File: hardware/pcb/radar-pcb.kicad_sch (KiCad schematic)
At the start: 36 parts, among them J1 DC 5,5x2,5 mm (+ w srodku), J2 DevKit J1, J3 DevKit J3, J4 HC-SR04 (kabel): VCC TRIG ECH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, J5 Serwo SG90 (kabel): GND +5V S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, J6 MAX7219 Elegoo: VCC GND DIN C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, J7 OLED SH1106: VCC GND SCK SDA, J8 Buzzer: + -, J9 Przycisk zewnetrzny, Q1 AO3401A (P-MOSFET), Q2 MMBT3904, SW1 Przycisk ON/standby, U1 SN74AHCT125N

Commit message: PCB: routed two-layer board, DRC clean, one-command rebuild
66 x 128 mm board generated from the schematic netlist with planned
placement for all 36 parts, routed with Freerouting, GND pours on both
layers. DRC with schematic parity: 0 errors, 0 unconnected, 0 parity
issues (silkscreen warnings only). build_all.sh regenerates everything.

Co-Authored-By: Claude Opus 5.5 <noreply@anthropic.com>
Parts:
- TP1, TP2, TP3, TP4, TP5: now left out of the parts list

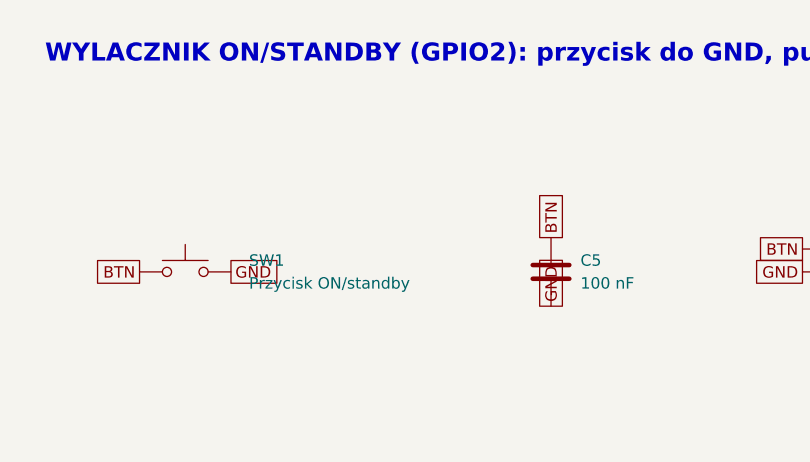
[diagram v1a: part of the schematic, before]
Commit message: PCB: silkscreen pin labels, side-actuated button, verification dimensions
Every connector is labelled with module and pin names, the DevKit sockets
with all 32 pin names on the back, parts with reference and value plus
polarity marks. ON/STANDBY uses a right-angle PTS645 switch at the left
edge. Dimensions W1-W12 to verify are drawn on Dwgs.User/Cmts.User for
the 1:1 verification PDF. DRC: 0 errors, schematic parity clean.

Co-Authored-By: Claude Opus 5.5 <noreply@anthropic.com>
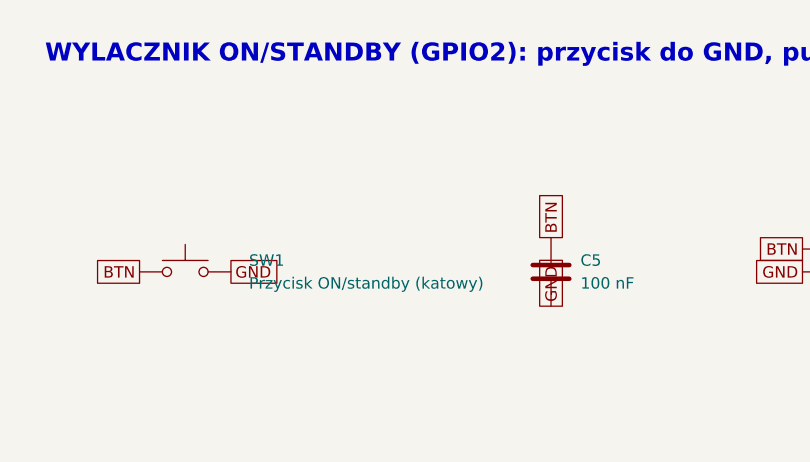
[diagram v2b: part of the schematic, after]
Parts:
- SW1: value Przycisk ON/standby -> Przycisk ON/standby (katowy); footprint Button_Switch_THT:SW_PUSH_6mm -> Button_Switch_THT:SW_Tactile_SPST_Angled_PTS645Vx58-2LFS

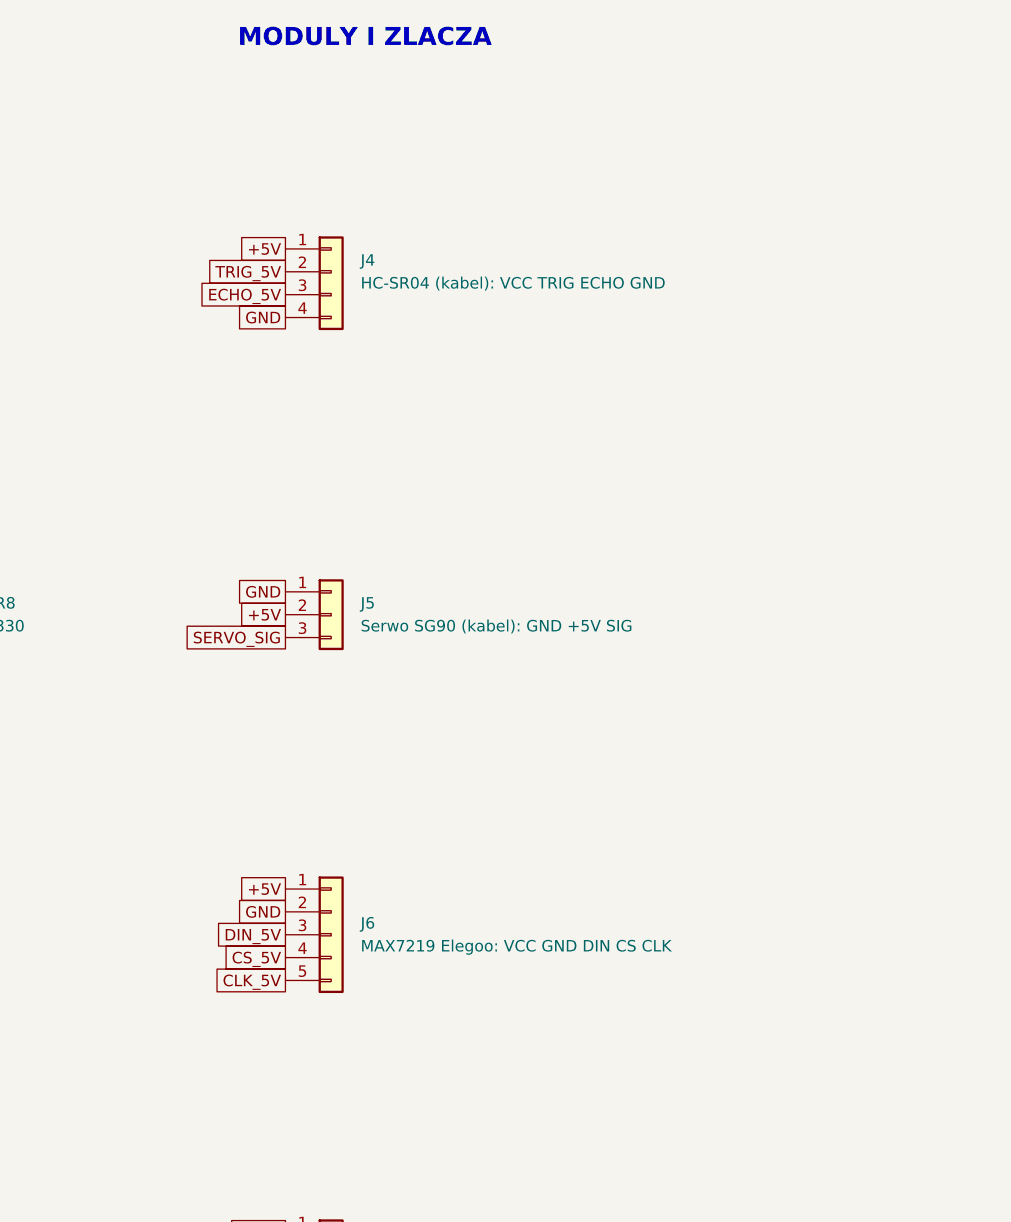
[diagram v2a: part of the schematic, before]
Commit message: PCB: sonar supply RC filter, series resistors and decoupling for the matrix
Breadboard tests showed MAX7219 row switching and bus traffic causing false
HC-SR04 echoes. Adds R11 10R with C6 100uF and C7 100nF on the sonar supply,
100R series resistors R12-R14 on DIN/CLK/CS and C8/C9 at the MAX7219 socket.
DRC with schematic parity: 0 errors. Adds export_docs.sh for renders and the
verification PDF.

Co-Authored-By: Claude Opus 5.5 <noreply@anthropic.com>
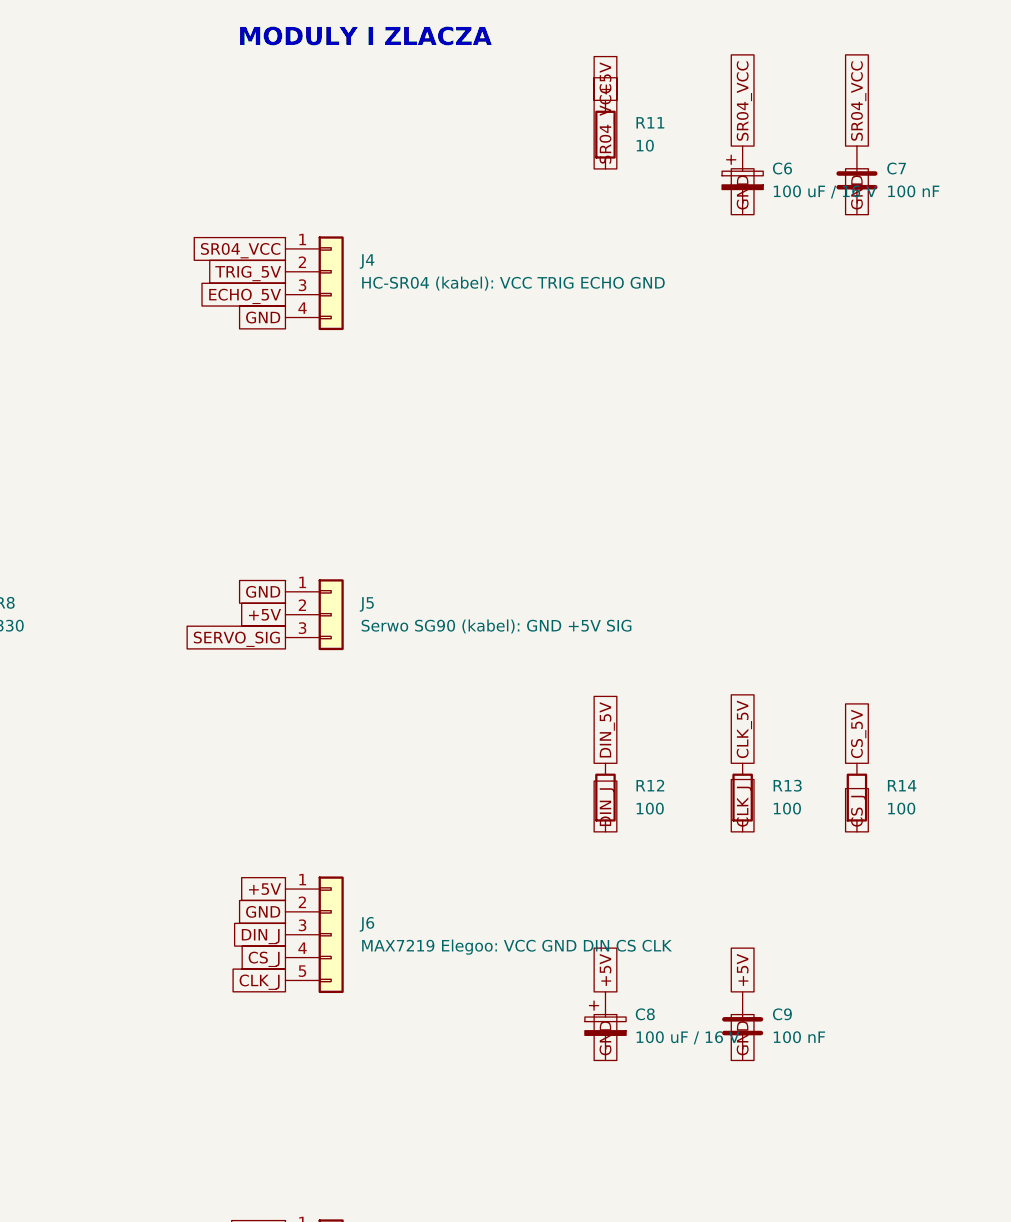
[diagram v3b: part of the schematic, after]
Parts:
- added C6, C8: 100 uF / 16 V, Capacitor_THT:CP_Radial_D6.3mm_P2.50mm, symbol Device:C_Polarized
- added C7, C9: 100 nF, Capacitor_SMD:C_0805_2012Metric, symbol Device:C
- added R11: 10, Resistor_SMD:R_0805_2012Metric, symbol Device:R
- added R12, R13, R14: 100, Resistor_SMD:R_0805_2012Metric, symbol Device:R
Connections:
- net +5V: now also C8.1, C9.1, R11.1; no longer J4.1 (Pin_1)
- net CLK_5V: now also R13.1; no longer J6.5 (Pin_5)
- net CS_5V: now also R14.1; no longer J6.4 (Pin_4)
- net DIN_5V: now also R12.1; no longer J6.3 (Pin_3)
- net GND: now also C6.2, C7.2, C8.2, C9.2
- new net CLK_J: J6.5 (Pin_5), R13.2
- new net CS_J: J6.4 (Pin_4), R14.2
- new net DIN_J: J6.3 (Pin_3), R12.2
- new net SR04_VCC: C6.1, C7.1, J4.1 (Pin_1), R11.2

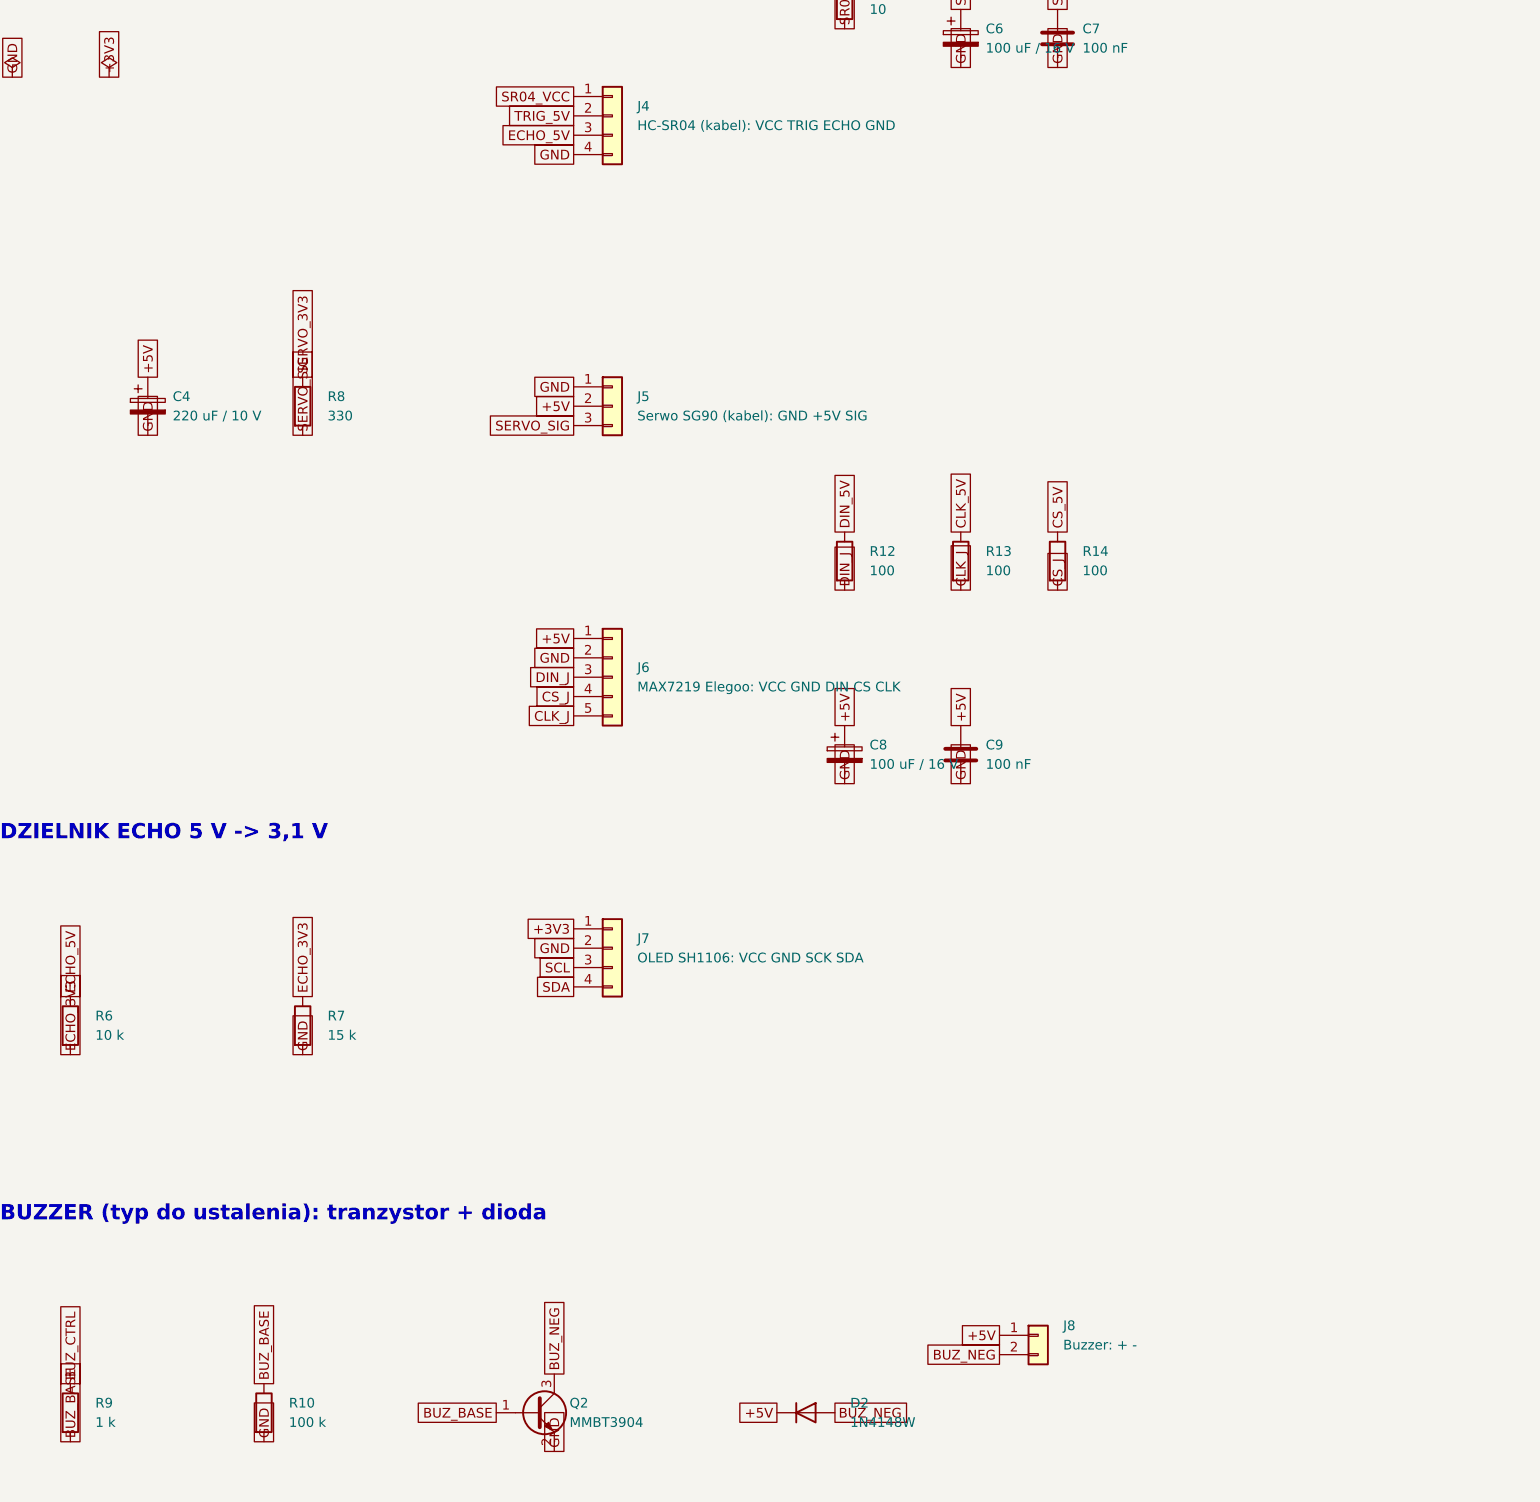
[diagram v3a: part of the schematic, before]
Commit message: PCB: servo supply isolation and decoupling, servo signal pull-down, buzzer decoupling
Co-Authored-By: Claude Sonnet 5.5 <noreply@anthropic.com>
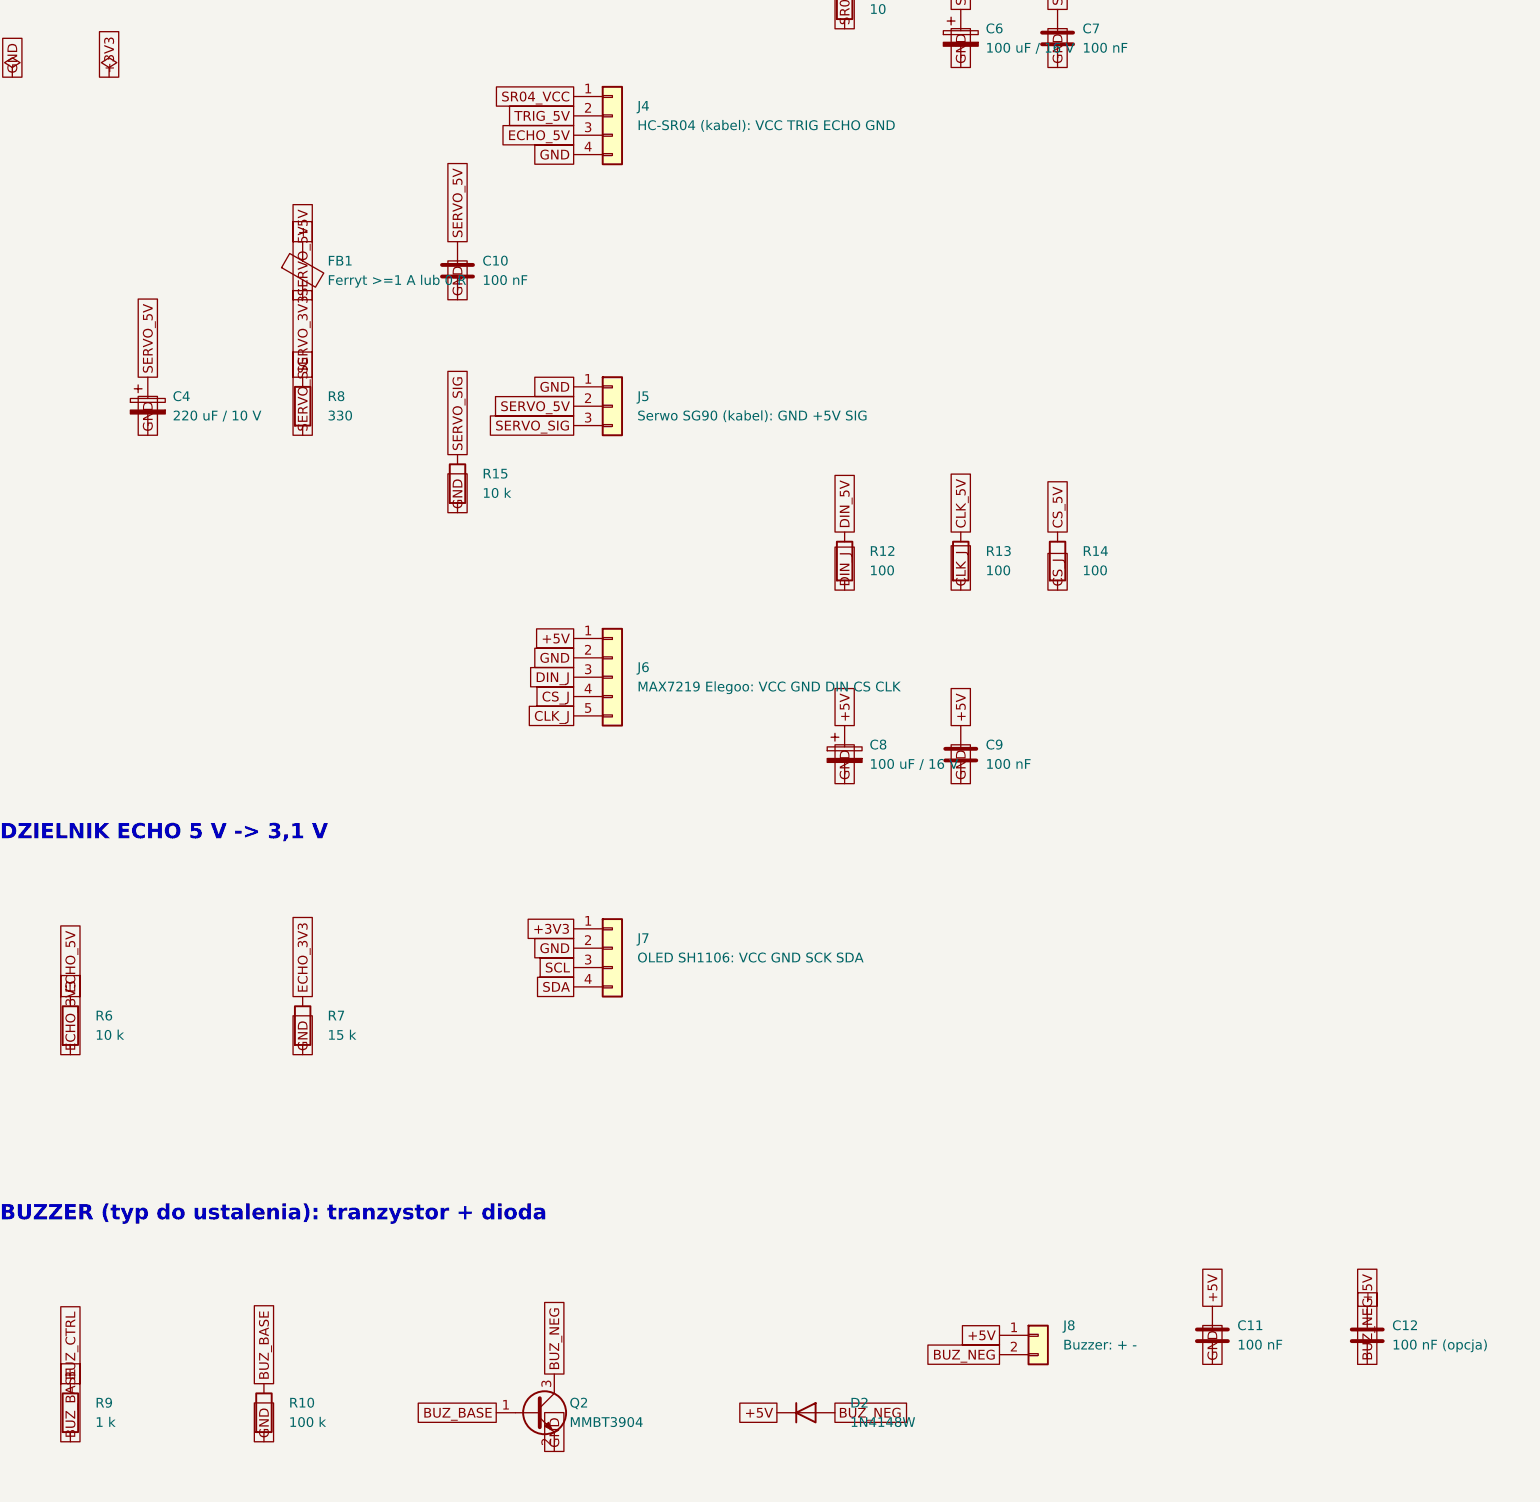
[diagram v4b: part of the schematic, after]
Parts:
- added C10, C11: 100 nF, Capacitor_SMD:C_0805_2012Metric, symbol Device:C
- added C12: 100 nF (opcja), Capacitor_SMD:C_0805_2012Metric, symbol Device:C
- added FB1: Ferryt >=1 A lub 0 R, Inductor_SMD:L_0805_2012Metric, symbol Device:FerriteBead
- added R15: 10 k, Resistor_SMD:R_0805_2012Metric, symbol Device:R
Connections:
- net +5V: now also C11.1, C12.1, FB1.1; no longer C4.1, J5.2 (Pin_2)
- net BUZ_NEG: now also C12.2
- net GND: now also C10.2, C11.2, R15.2
- net SERVO_SIG: now also R15.1
- new net SERVO_5V: C10.1, C4.1, FB1.2, J5.2 (Pin_2)
